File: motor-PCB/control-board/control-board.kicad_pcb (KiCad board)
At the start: 2 copper layers, 80.2 x 57 mm, 22 parts, among them J1 Power Input, J2 Motor, J3 Optocoupler, J4 Conn_01x04, J5 Connection with second PCB, U1 LM7812_TO220, U2 INA219BxDCN, U3 LM7805_TO220, U4 TMP117xxDRV

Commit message: Final Control-Board
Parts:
- removed C8: 0.1u, Capacitor_THT:C_Disc_D5.0mm_W2.5mm_P2.50mm
- removed J4: Conn_01x04, Custom:1x04_P2.54mm_Horizontal
- C3: value 0.1u -> 100nF
- C6: value 10u -> 10µF
- C7: value 0.1u -> 0.1µF
- J1, J2: footprint Custom:1x02_P2.54mm_Horizontal -> TerminalBlock_CUI:TerminalBlock_CUI_TB007-508-02_1x02_P5.08mm_Horizontal
- moved J1 3.05 mm to (85.1, 73.5)
- moved J2 2.34 mm to (149.9, 73.2)
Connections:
- A1 pad 11: unconnected-(A1-D8-Pad11) -> D8
- A1 pad 6: D3 -> unconnected-(A1-D3-Pad6)
- A1 pad 8: D5 -> unconnected-(A1-D5-Pad8)
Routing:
- net D3: track 38.1 -> 0.00 mm
- net D5: track 33.5 -> 0.00 mm
- net D11: track 86.4 -> 102.5 mm
- net +5V: track 141.1 -> 133.2 mm
- net Net-(J1-Pin_1): track 24.5 -> 20.3 mm
- net Net-(D1-K): track 62.6 -> 60.2 mm
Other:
- board size 80.2 x 57 mm -> 80.2 x 56.8 mm
- board text removed: "+"
- board text removed: "-"
- board text removed: "D3"
- board text removed: "D5"
- board text removed: "GND"
- board text removed: "Motor"
- board text removed: "Team 7"

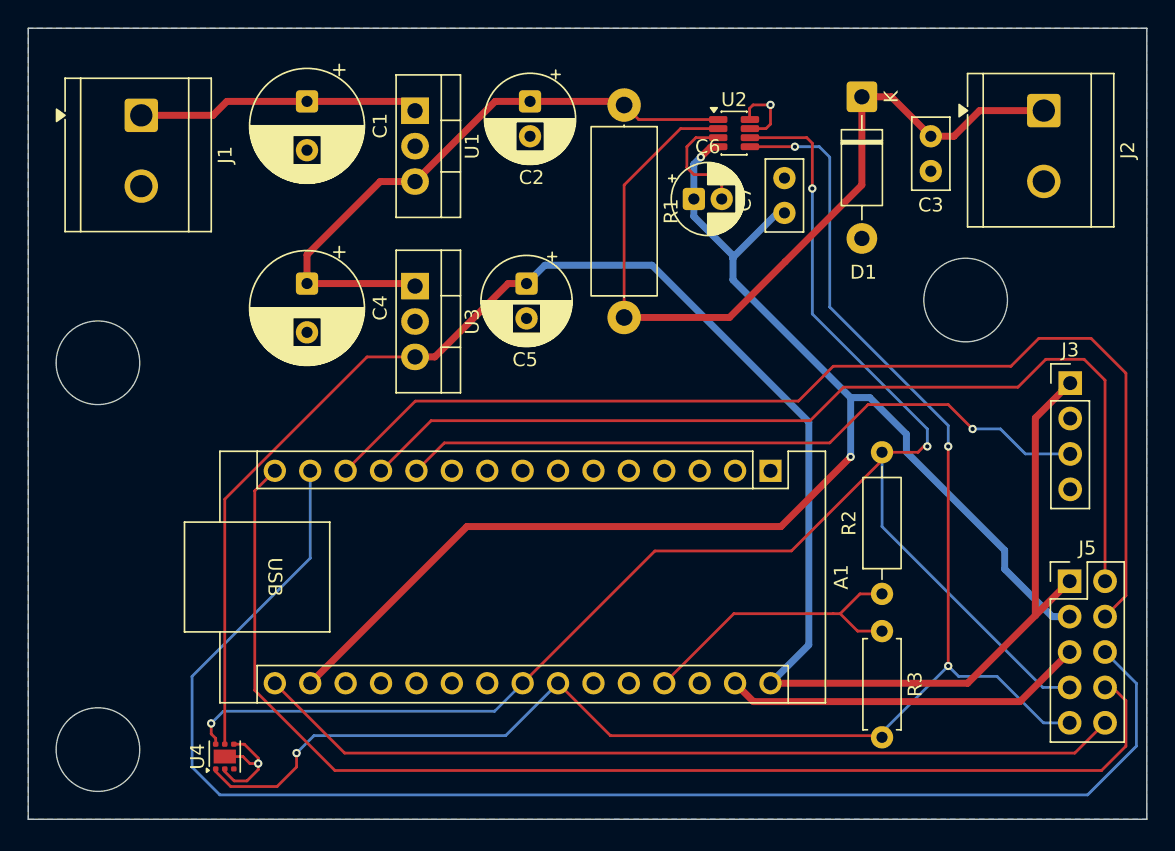
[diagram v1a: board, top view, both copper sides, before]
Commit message: added a missing capacitor in the control-board. Added pins to be able to control the heating pad and fan and text. In the generator changed the transistor layout and also added text
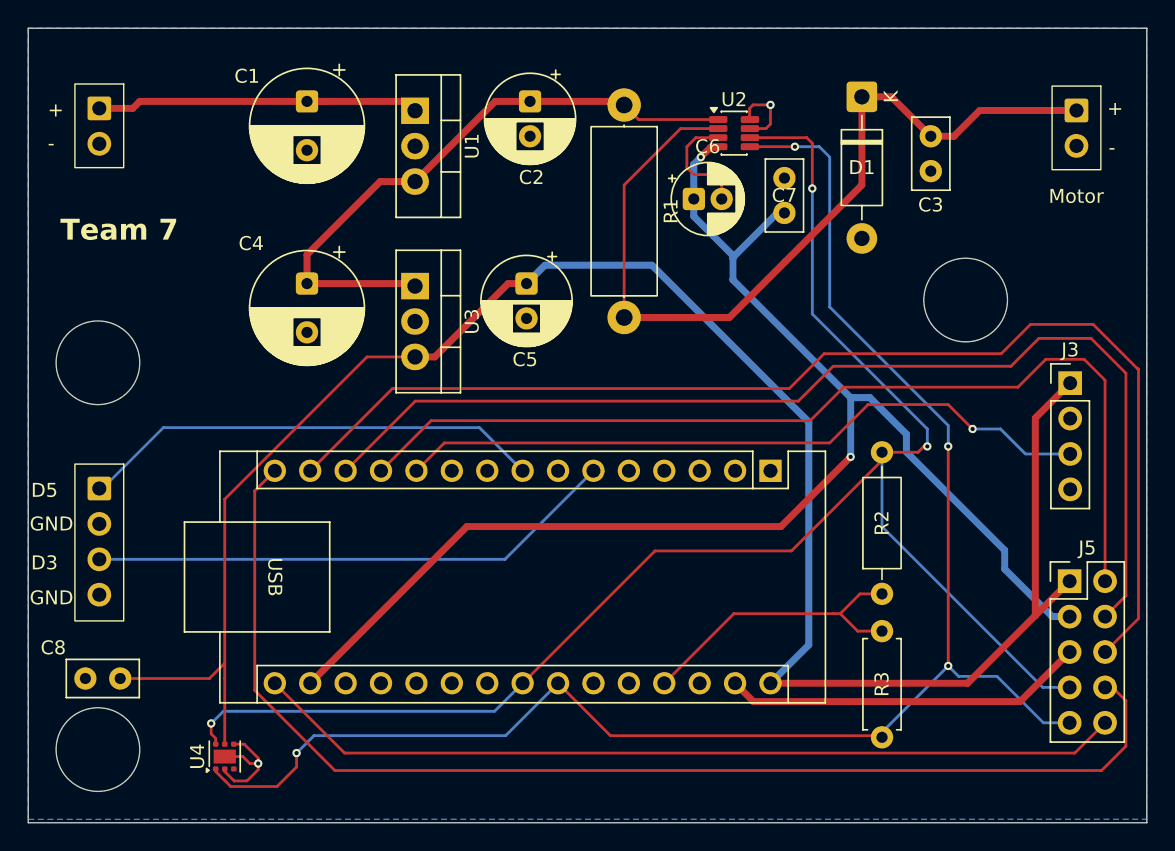
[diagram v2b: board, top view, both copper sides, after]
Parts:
- added C8: 0.1u, Capacitor_THT:C_Disc_D5.0mm_W2.5mm_P2.50mm, F.Cu at (83.6, 113.9)
- added J4: Conn_01x04, Custom:1x04_P2.54mm_Horizontal, F.Cu at (82.1, 100.3)
- C3: value 100nF -> 0.1u
- C6: value 10µF -> 10u
- C7: value 0.1µF -> 0.1u
- J1, J2: footprint TerminalBlock_CUI:TerminalBlock_CUI_TB007-508-02_1x02_P5.08mm_Horizontal -> Custom:1x02_P2.54mm_Horizontal
- moved J1 3.05 mm to (82.1, 73.0)
- moved J2 2.34 mm to (152.2, 73.2)
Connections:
- A1 pad 11: D8 -> unconnected-(A1-D8-Pad11)
- A1 pad 6: unconnected-(A1-D3-Pad6) -> D3
- A1 pad 8: unconnected-(A1-D5-Pad8) -> D5
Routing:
- net D3: track 0.00 -> 38.1 mm
- net D5: track 0.00 -> 33.5 mm
- net D11: track 102.5 -> 86.4 mm
- net +5V: track 133.2 -> 141.1 mm
- net Net-(J1-Pin_1): track 20.3 -> 24.5 mm
- net Net-(D1-K): track 60.2 -> 62.6 mm
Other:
- board size 80.2 x 56.8 mm -> 80.2 x 57 mm
- board text added: "+"
- board text added: "-"
- board text added: "D3"
- board text added: "D5"
- board text added: "GND"
- board text added: "Motor"
- board text added: "Team 7"
